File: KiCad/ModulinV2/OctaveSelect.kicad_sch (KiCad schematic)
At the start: 30 parts, among them IC21 SN74LV10ADR, IC22 SN74LV10ADR, IC23 SN74LV10ADR, IC24 SN74HC193DR, IC25 TMUX4051DYYRQ1

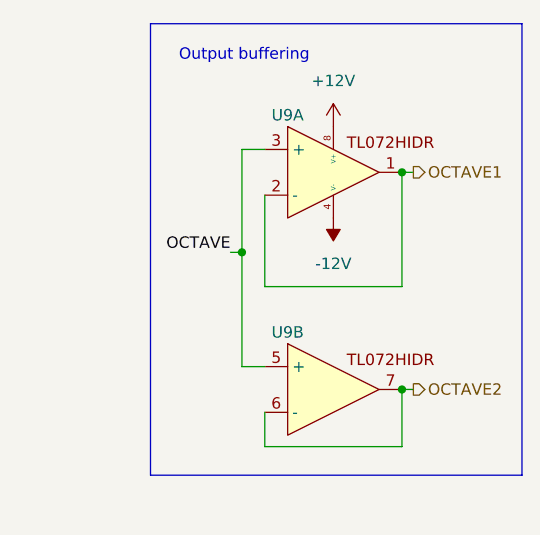
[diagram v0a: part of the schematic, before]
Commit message: Updated TL074 and 72 symbols
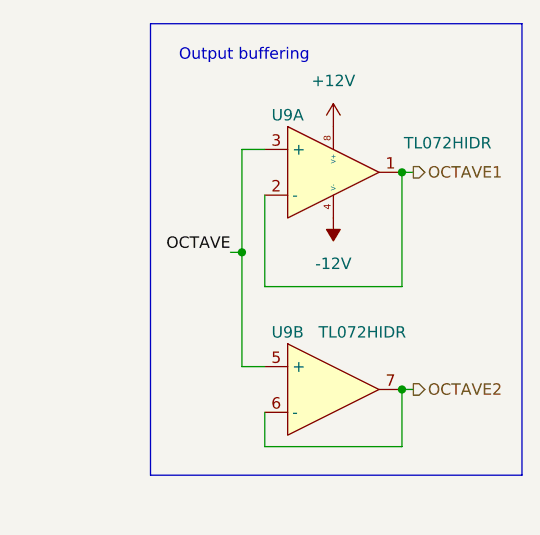
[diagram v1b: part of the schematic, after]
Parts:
- U9: value ~ -> TL072HIDR
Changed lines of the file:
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@@
 			)
 		)
-		(property "Value" "~"
+		(property "Value" "TL072HIDR"
 			(at 266.1055 48.26 0)
 			(effects
@@
 			)
 		)
-		(property "Value" "~"
+		(property "Value" "TL072HIDR"
 			(at 275.59 27.2349 0)
 			(effects

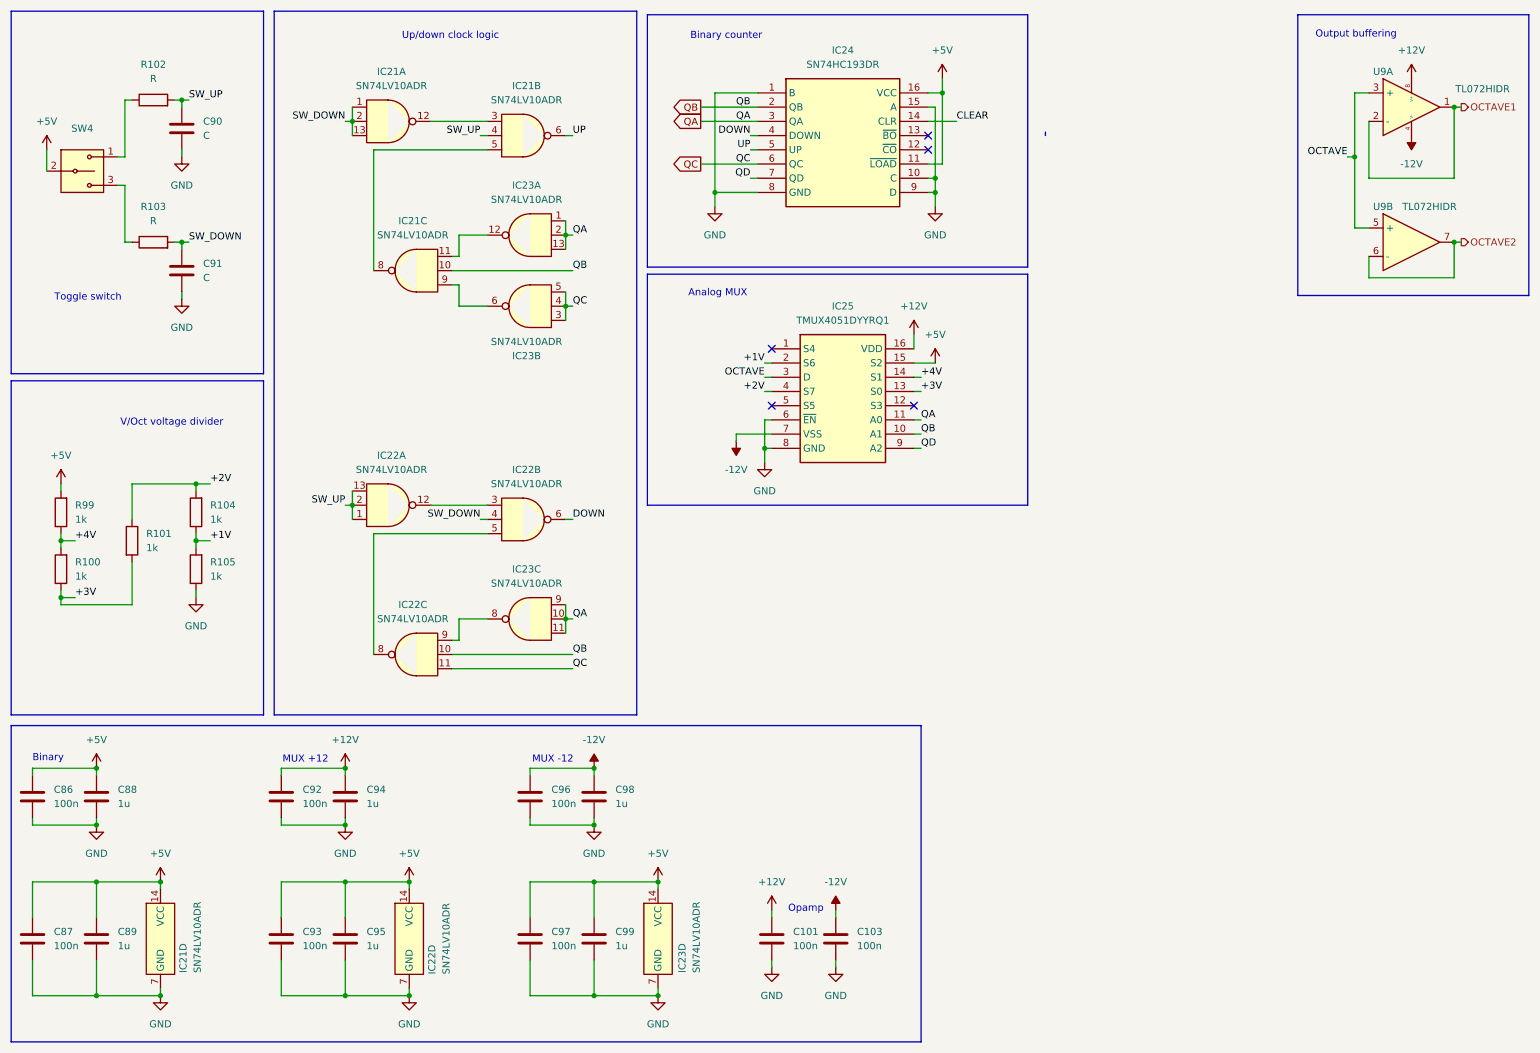
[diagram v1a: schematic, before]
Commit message: Fixed library issues and assigned most footprints
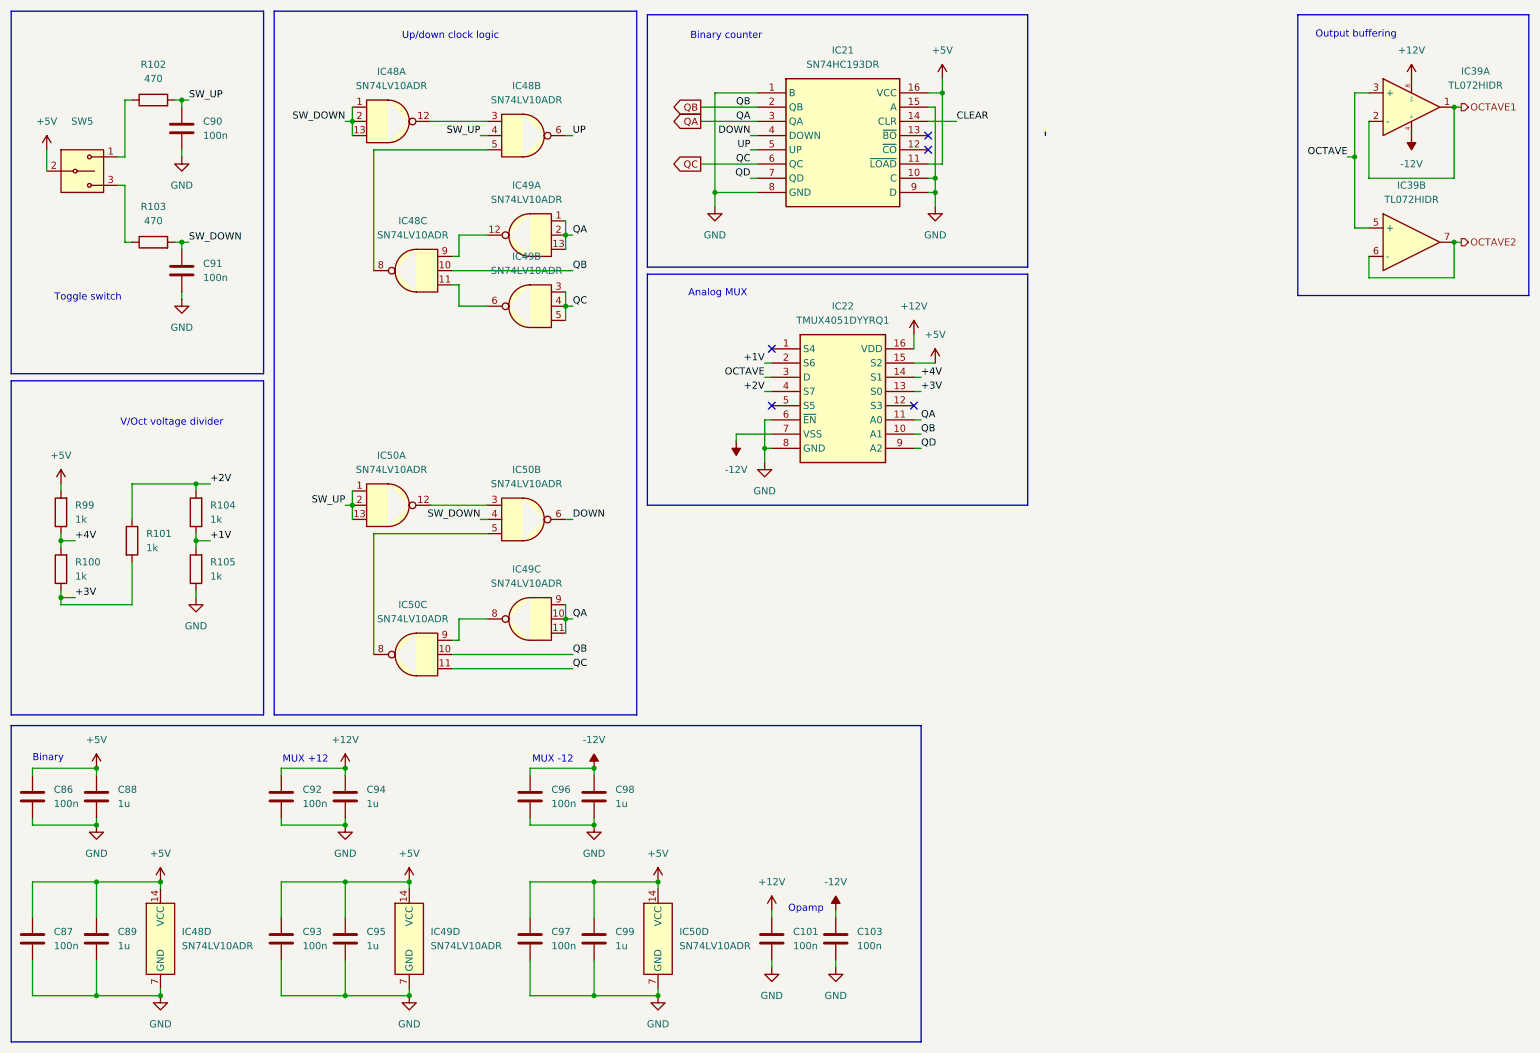
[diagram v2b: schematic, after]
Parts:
- removed IC21, IC22, IC23: SN74LV10ADR, symbol SN74LV10ADR:SN74LV10ADRx3
- removed IC24: SN74HC193DR, SOIC127P600X175-16N, symbol SN74HC193DR:SN74HC193DR
- removed IC25: TMUX4051DYYRQ1, SOP50P326X110-16N, symbol TMUX4051DYYRQ1:TMUX4051DYYRQ1
- removed SW4: ~, symbol RB14DE1100:RB14DE1100
- removed U9: TL072HIDR, symbol TL072HIDR:TL072HIDRx2
- added IC21: SN74HC193DR, SamacSys_Parts:SOIC127P600X175-16N, symbol SamacSys_Parts:SN74HC193DR
- added IC22: TMUX4051DYYRQ1, SamacSys_Parts:SOP50P326X110-16N, symbol SamacSys_Parts:TMUX4051DYYRQ1
- added IC39: TL072HIDR, SamacSys_Parts:SOIC127P600X175-8N, symbol SamacSys_Parts:TL072HIDR
- added IC48, IC49, IC50: SN74LV10ADR, SamacSys_Parts:SOIC127P600X175-14N, symbol SamacSys_Parts:SN74LV10ADR
- added SW5: ~, symbol SamacSys_Parts:RB14DE1100
- C90, C91: value C -> 100n
- R102, R103: value R -> 470
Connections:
- net +12V: now also IC22.16 (VDD), IC39.8 (V+)
- net +1V: now also IC22.2 (S6)
- net +2V: now also IC22.4 (S7)
- net +3V: now also IC22.13 (S0)
- net +4V: now also IC22.14 (S1)
- net +5V: now also IC21.11 (~{LOAD}), IC21.16 (VCC), IC22.15 (S2), IC48.14 (VCC), IC49.14 (VCC), IC50.14 (VCC), SW5.2
- net -12V: now also IC22.7 (VSS), IC39.4 (V-)
- net CLEAR: now also IC21.14 (CLR)
- net DOWN: now also IC21.4 (DOWN), IC50.6
- net GND: now also IC21.1 (B), IC21.10 (C), IC21.15 (A), IC21.8 (GND), IC21.9 (D), IC22.6 (~{EN}), IC22.8 (GND), IC48.7 (GND), IC49.7 (GND), IC50.7 (GND)
- net OCTAVE: now also IC22.3 (D), IC39.3 (+), IC39.5 (+)
- net OCTAVE1: now also IC39.1, IC39.2 (-)
- net OCTAVE2: now also IC39.6 (-), IC39.7
- net QA: now also IC21.3 (QA), IC22.11 (A0), IC49.1, IC49.10, IC49.11, IC49.13, IC49.2, IC49.9
- net QB: now also IC21.2 (QB), IC22.10 (A1), IC48.10, IC50.10
- net QC: now also IC21.6 (QC), IC49.3, IC49.4, IC49.5, IC50.11
- net QD: now also IC21.7 (QD), IC22.9 (A2)
- net SW_DOWN: now also IC48.1, IC48.13, IC48.2, IC50.4
- net SW_UP: now also IC48.4, IC50.1, IC50.13, IC50.2
- net UP: now also IC21.5 (UP), IC48.6
- net at R102.1: now also SW5.1
- net at R103.1: now also SW5.3
- new net: IC48.12, IC48.3
- new net: IC48.11, IC49.6
- new net: IC48.5, IC48.8
- new net: IC48.9, IC49.12
- new net: IC50.5, IC50.8
- new net: IC49.8, IC50.9
- new net: IC50.12, IC50.3

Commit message: Changed switch for the boot and nrst. Fixed the GATE interface trigger
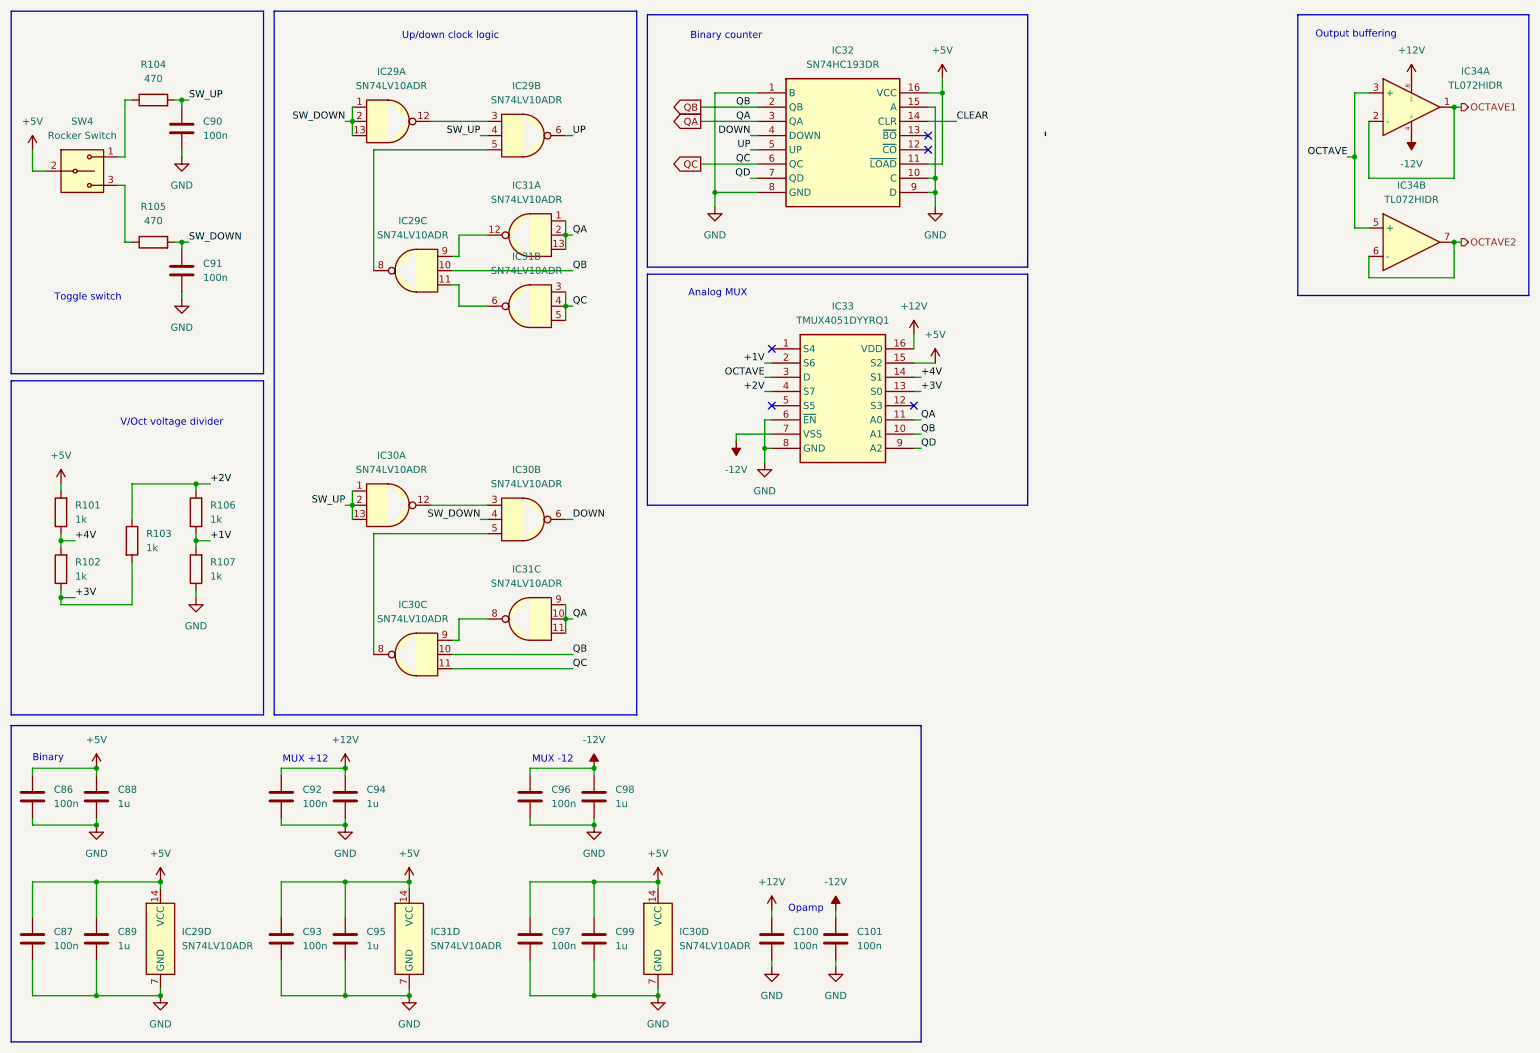
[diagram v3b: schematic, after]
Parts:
- SW4: renamed from SW5; value ~ -> Rocker Switch
- renumbered C101 to C100, C103 to C101, IC48 to IC29, IC50 to IC30, IC49 to IC31, IC21 to IC32, IC22 to IC33, IC39 to IC34, R99 to R101, R100 to R102, R101 to R103, R102 to R104, R103 to R105, R104 to R106, R105 to R107

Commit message: Started adding footprints for capacitors
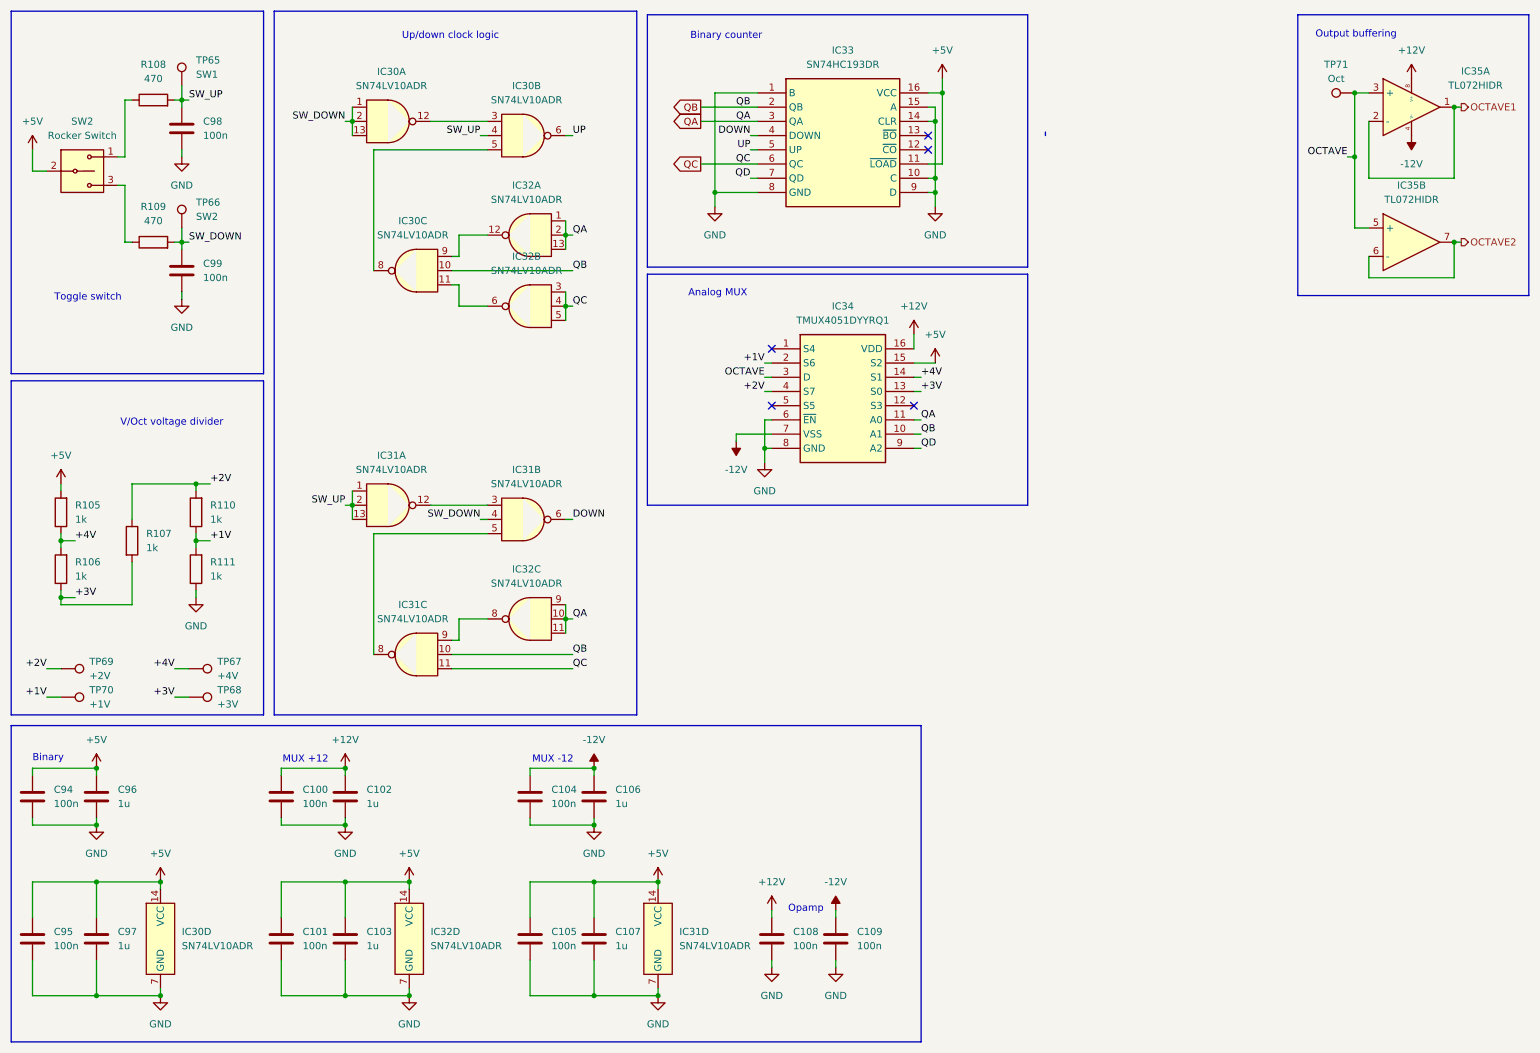
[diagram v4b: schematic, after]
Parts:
- added TP65: SW1, SamacSys_Parts:TestPointLoop, symbol Connector:TestPoint
- added TP66: SW2, SamacSys_Parts:TestPointLoop, symbol Connector:TestPoint
- added TP67: +4V, SamacSys_Parts:TestPointLoop, symbol Connector:TestPoint
- added TP68: +3V, SamacSys_Parts:TestPointLoop, symbol Connector:TestPoint
- added TP69: +2V, SamacSys_Parts:TestPointLoop, symbol Connector:TestPoint
- added TP70: +1V, SamacSys_Parts:TestPointLoop, symbol Connector:TestPoint
- added TP71: Oct, SamacSys_Parts:TestPointLoop, symbol Connector:TestPoint
- C100: renamed from C92; footprint (none) -> SamacSys_Parts:CAPC1608X90N
- C101: renamed from C93; footprint (none) -> SamacSys_Parts:CAPC1608X90N
- C102: renamed from C94; footprint (none) -> SamacSys_Parts:CAPC1608X95N
- C103: renamed from C95; footprint (none) -> SamacSys_Parts:CAPC1608X95N
- C104: renamed from C96; footprint (none) -> SamacSys_Parts:CAPC1608X90N
- C105: renamed from C97; footprint (none) -> SamacSys_Parts:CAPC1608X90N
- C106: renamed from C98; footprint (none) -> SamacSys_Parts:CAPC1608X95N
- C107: renamed from C99; footprint (none) -> SamacSys_Parts:CAPC1608X95N
- C108: renamed from C100; footprint (none) -> SamacSys_Parts:CAPC1608X90N
- C109: renamed from C101; footprint (none) -> SamacSys_Parts:CAPC1608X90N
- C94: renamed from C86; footprint (none) -> SamacSys_Parts:CAPC1608X90N
- C95: renamed from C87; footprint (none) -> SamacSys_Parts:CAPC1608X90N
- C96: renamed from C88; footprint (none) -> SamacSys_Parts:CAPC1608X95N
- C97: renamed from C89; footprint (none) -> SamacSys_Parts:CAPC1608X95N
- C98: renamed from C90; footprint (none) -> SamacSys_Parts:CAPC1608X90N
- C99: renamed from C91; footprint (none) -> SamacSys_Parts:CAPC1608X90N
- SW2: renamed from SW4; footprint (none) -> SamacSys_Parts:RB14DE1100
- renumbered IC29 to IC30, IC30 to IC31, IC31 to IC32, IC32 to IC33, IC33 to IC34, IC34 to IC35, R101 to R105, R102 to R106, R103 to R107, R104 to R108, R105 to R109, R106 to R110, R107 to R111
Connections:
- net CLEAR is gone; now on net GND: IC33.14 (CLR)
- net +1V: now also TP70.1
- net +2V: now also TP69.1
- net +3V: now also TP68.1
- net +4V: now also TP67.1
- net OCTAVE: now also TP71.1
- net SW_DOWN: now also TP66.1
- net SW_UP: now also TP65.1
